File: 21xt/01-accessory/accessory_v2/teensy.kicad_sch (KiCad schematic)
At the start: 15 parts, among them T1 749013011, U1 DEV-16771

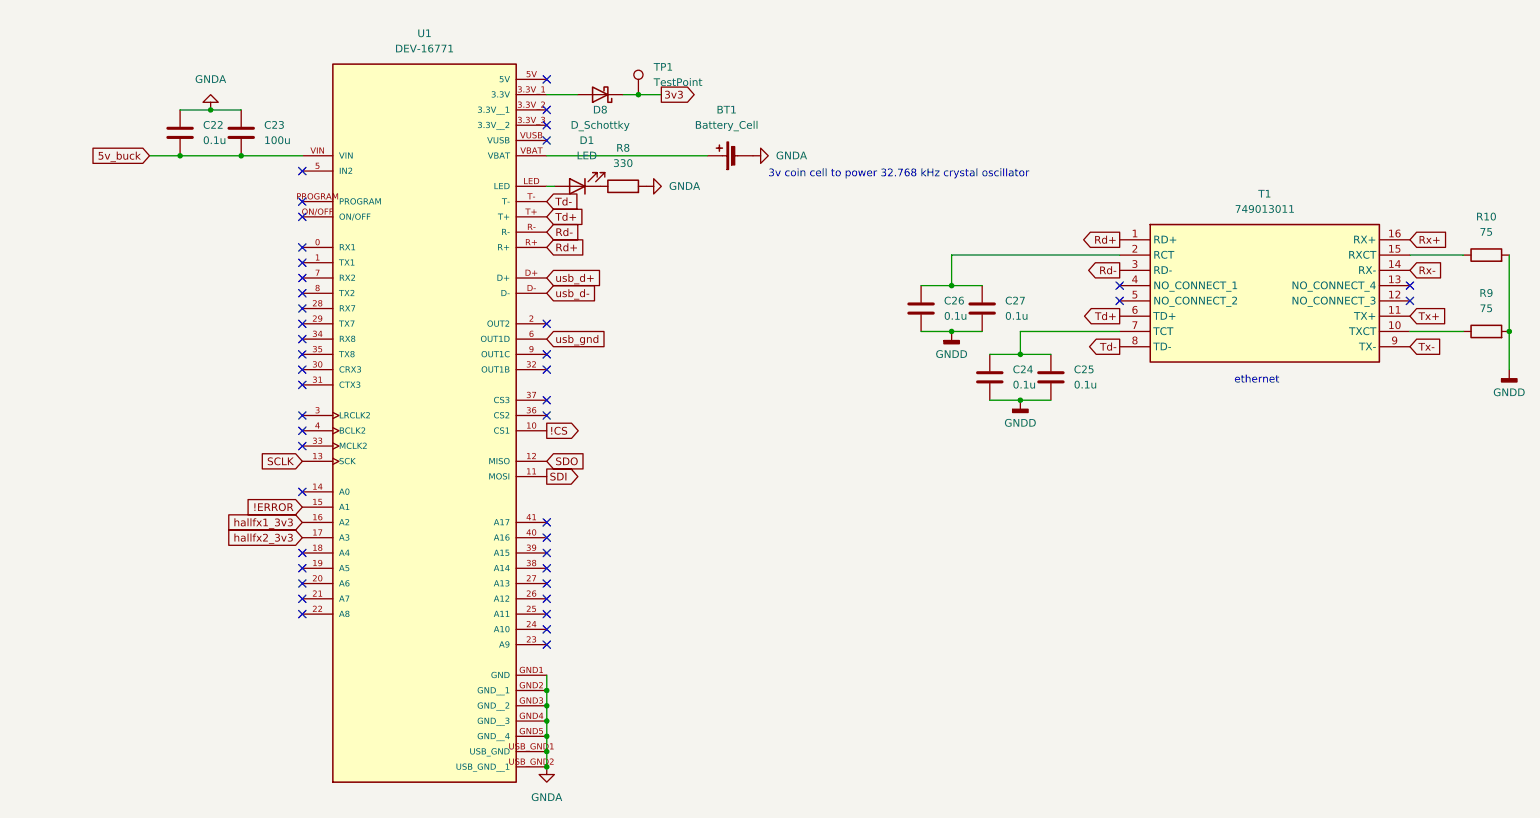
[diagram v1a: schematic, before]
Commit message: Accessory V2 schematic almost done, only missing TVS diodes and checking
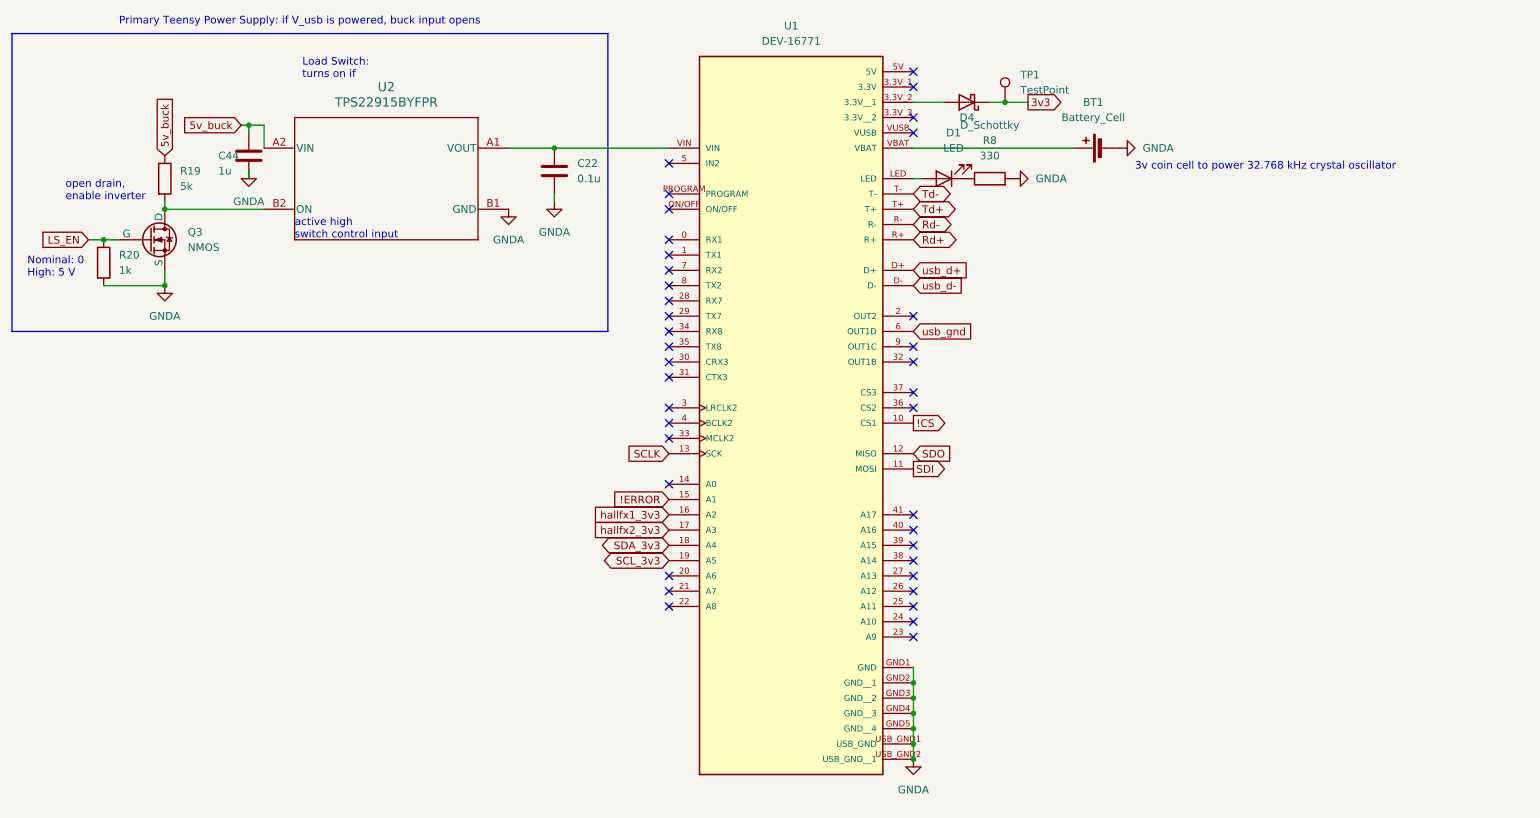
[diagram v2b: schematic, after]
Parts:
- removed C23: 100u, Capacitor_SMD:C_1206_3216Metric, symbol Device:C
- removed C24, C25, C26, C27: 0.1u, Capacitor_SMD:C_0603_1608Metric, symbol Device:C
- removed D8: D_Schottky, Diode_SMD:D_0603_1608Metric, symbol Device:D_Schottky
- removed R10, R9: 75, Resistor_SMD:R_0603_1608Metric, symbol Device:R
- removed T1: 749013011, 21xt_footprints:749013011, symbol 21xt_symbols:749013011
- added C44: 1u, Capacitor_SMD:C_0603_1608Metric, symbol Device:C
- added D4: D_Schottky, Diode_SMD:D_0603_1608Metric, symbol Device:D_Schottky
- added Q3: NMOS, symbol Simulation_SPICE:NMOS
- added R19: 5k, symbol Device:R
- added R20: 1k, symbol Device:R
- added U2: TPS22915BYFPR, 21xt_footprints:YFP0004AAAA, symbol 21xt_symbols:TPS22915BYFPR
- BT1: footprint (none) -> Battery:BatteryHolder_Keystone_1060_1x2032
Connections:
- net 3v3: now also D4.1 (K)
- net 5v_buck: now also C44.2, R19.1, U2.A2 (VIN); no longer C22.2, U1.VIN
- net GNDA: now also C44.1, Q3.3 (S), R20.2, U2.B1 (GND)
- net SDA_3v3: now reaches U1.18 (A4)
- net SCL_3v3: now reaches U1.19 (A5)
- net at U1.3.3V_2 (3.3V__1): now also D4.2 (A)
- new net: Q3.1 (D), R19.2, U2.B2 (ON)
- new net: C22.2, U1.VIN, U2.A1 (VOUT)
- new net LS_EN: Q3.2 (G), R20.1
- no-connect marks 44 -> 38
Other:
- note added: "Load Switch: turns on if"
- note added: "Nominal: 0 High: 5 V"
- note added: "Primary Teensy Power Supply: if V_usb is powered, buck input opens"
- note added: "active high switch control input"
- note added: "open drain, enable inverter"
- note removed: "ethernet"
- moved on the sheet: BT1, D1, R8, U1

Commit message: comments for revision added
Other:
- note added: "actually is this intended for the usb connector on the teensy? because if it is, then the usb cannot back power the board and blow up your buck converter if you leave the shottky i told you to remove, but even then, the buck converter can blow up the USB line or just overvolt it because the usb does not get disconnected"
- note added: "also if we have no power on the car, but have power on usb, will this turn on? it seems to me that if the connector is plugged in then ls_en is grounded so the gate opens, but there is no power"
- note added: "also you need to add the 4 pin m8 connector for getting the usb power to the teensy, though I suppose this functions for powering the teensy via the usb connector on the teensy board"
- note added: "i dont think these are the right connections for the usb grounding"
- note added: "i dont think you have connected all of the digital pins d4,5,6"
- note added: "i think i am impartial to the case where we are connecting to the teensy via the microusb on the board but if you wanted to have a proper load switch for the m8 connector that you are exposing, then i think you would need the load switch on that line: ie if the ls_en pin is activated then turn off the m8 power,"
- note added: "it becomes a bit more complicated if you wanted to support the USB connector on the board, in that case, you probably have to have the USB power always be the source for everything when its plugged in or have to snip the trace in order to control that connection, at the very least i think you have to model the m8 connector and determine which of that connector and the big bulkhead are dominant an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"
- note added: "or hallfx3"
- note added: "shouldnt the buck converter have precedent over the usb power for example: if the usb is higher voltage than buck, then the signals will exceed the threshold for levels on the usb, if the buck converter is higher though, then the signalling on the usb side may not reach high enough. also, we want no interruption when you plug in and need to switch tho id if that is significant"
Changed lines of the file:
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@@
     (stroke (width 0) (type default))
+  )
+  (arc (start 313.69 53.34) (mid 254.2256 96.5696) (end 181.61 85.09)
+    (stroke (width 0) (type default))
+    (fill (type none))
+  )
+  (arc (start 312.42 54.61) (mid 243.3139 81.7468) (end 175.26 52.07)
+    (stroke (width 0) (type default))
+    (fill (type none))
+  )
+  (arc (start -6.35 22.86) (mid 25.5167 29.747) (end 43.18 57.15)
+    (stroke (width 0) (type default))
+    (fill (type none))
+  )
+  (arc (start 313.69 109.22) (mid 222.2951 150.7967) (end 128.27 115.57)
+    (stroke (width 0) (type default))
+    (fill (type none))
+  )
+  (arc (start 313.69 54.61) (mid 263.349 134.2339) (end 171.45 154.94)
+    (stroke (width 0) (type default))
+    (fill (type none))
   )
   (rectangle (start 27.94 35.56) (end 127 85.09)
@@
     (effects (font (size 1.27 1.27)) (justify left bottom))
   )
+  (text "it becomes a bit more complicated if you wanted to support the USB\nconnector on the board, in that case, you probably have to have\nthe USB power always be the source for everything when its plugged\nin or have to snip the trace in order to control that connection,\nat the very least i think you have to model the m8 connector\nand determine which of that connector and the big bulkhead are dominant\nand possible just ignore the usb, but maximally, this would require two\nload switches and possibly snipping the connection, but i think we can\nget around that by just asuming the usb connector is only for off board\ncases and the primary modality of programming this guy is through the\nm8 connector"
+    (at -74.93 127 0)
+    (effects (font (size 1.27 1.27)) (justify left bottom))
+  )
   (text "Nominal: 0\nHigh: 5 V" (at 30.48 76.2 0)
+    (effects (font (size 1.27 1.27)) (justify left bottom))
+  )
+  (text "shouldnt the buck converter have precedent over the usb power\nfor example: if the usb is higher voltage than buck, then\nthe signals will exceed the threshold for levels on the usb,\nif the buck converter is higher though, then the signalling \non the usb side may not reach high enough. also, we want no\ninterruption when you plug in and need to switch tho id if \nthat is significant"
+    (at -71.12 21.59 0)
+    (effects (font (size 1.27 1.27)) (justify left bottom))
+  )
+  (text "actually is this intended for the usb connector\non the teensy? because if it is, then the usb\ncannot back power the board and blow up your \nbuck converter if you leave the shottky i told\nyou to remove, but even then, the buck converter\ncan blow up the USB line or just overvolt it\nbecause the usb does not get disconnected"
+    (at -80.01 72.39 0)
     (effects (font (size 1.27 1.27)) (justify left bottom))
   )
@@
     (effects (font (size 1.27 1.27)) (justify left bottom))
   )
+  (text "or hallfx3" (at 313.69 114.3 0)
+    (effects (font (size 1.27 1.27)) (justify left bottom))
+  )
+  (text "i dont think you have connected all of the digital pins d4,5,6"
+    (at 313.69 110.49 0)
+    (effects (font (size 1.27 1.27)) (justify left bottom))
+  )
+  (text "also you need to add the 4 pin m8 connector\nfor getting the usb power to the teensy,\nthough I suppose this functions for powering the teensy\nvia the usb connector on the teensy board"
+    (at -69.85 50.8 0)
+    (effects (font (size 1.27 1.27)) (justify left bottom))
+  )
+  (text "i think i am impartial to the case where we are connecting\nto the teensy via the microusb on the board but\nif you wanted to have a proper load switch for the\nm8 connector that you are exposing, then i think you would need\nthe load switch on that line: ie if the ls_en pin is activated\nthen turn off the m8 power,\n"
+    (at -78.74 97.79 0)
+    (effects (font (size 1.27 1.27)) (justify left bottom))
+  )
+  (text "i dont think these are the right connections for the usb grounding"
+    (at 317.5 54.61 0)
+    (effects (font (size 1.27 1.27)) (justify left bottom))
+  )
+  (text "also if we have no power on the car, but have power on usb, will this turn on?\nit seems to me that if the connector is plugged in then\nls_en is grounded so the gate opens, but there is no power "
+    (at -76.2 34.29 0)
+    (effects (font (size 1.27 1.27)) (justify left bottom))
+  )

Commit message: Addressed some comments
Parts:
- added R43, R44, R45, R47: 22, symbol Device:R
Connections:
- net !ERROR: now also U1.14 (A0); no longer U1.15 (A1)
- net SDI: now also R44.2; no longer U1.11 (MOSI)
- net D4_3v3: now reaches U1.0 (RX1)
- net D3_3v3: now reaches U1.1 (TX1)
- net D2_3v3: now reaches U1.26 (A12)
- net D1_3v3: now reaches U1.27 (A13)
- net !RESET: now reaches U1.35 (TX8)
- net !LDAC: now reaches U1.36 (CS2)
- net at U1.37 (CS3): now also R47.1
- net D6_3v3: now reaches U1.7 (RX2)
- net D5_3v3: now reaches U1.8 (TX2)
- net !CS: no longer names the net of U1.10 (CS1)
- net !CS: now also R45.1
- net SCLK: no longer names the net of U1.13 (SCK)
- net SCLK: now also R43.2
- net SDO renamed SDO_ADC
- net hallfx1_3v3: no longer names the net of U1.16 (A2)
- net hallfx2_3v3: no longer names the net of U1.17 (A3)
- new net: R44.1, U1.11 (MOSI)
- new net !CS_ADC: R45.2
- new net !CS_DAC: R47.2
- new net SCK: R43.1
- no-connect marks 38 -> 28
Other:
- note removed: "i dont think you have connected all of the digital pins d4,5,6"
- note removed: "or hallfx3"

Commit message: added files
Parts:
- removed D4: D_Schottky, Diode_SMD:D_0603_1608Metric, symbol Device:D_Schottky
- removed Q3: NMOS, symbol Simulation_SPICE:NMOS
- added Q3: BSS138, Package_TO_SOT_SMD:SOT-23, symbol Transistor_FET:BSS138
- C22, C44: footprint Capacitor_SMD:C_0603_1608Metric -> Capacitor_SMD:C_0402_1005Metric
- R19, R20, R43, R44, R45, R47: footprint (none) -> Resistor_SMD:R_0603_1608Metric
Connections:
- net 3v3: now also U1.3.3V_2 (3.3V__1)
- net GNDA: now also Q3.2 (S)
- net LS_EN: now also Q3.1 (G)
- net at R19.2, U2.B2 (ON): now also Q3.3 (D)
- net at U1.23 (A9): now also D1.2 (A)
- net GPIO/INT1_3v3: now reaches U1.24 (A10)
- net GPIO/INT2_3v3: now reaches U1.25 (A11)
- net at U1.LED: no longer D1.2 (A)
- net 5v_usb: now reaches U1.VUSB
- net usb_d+: no longer names the net of U1.D+
- net usb_d-: no longer names the net of U1.D-
- net usb_gnd: no longer names the net of U1.6 (OUT1D)
- no-connect marks 28 -> 31
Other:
- note added: "LS_EN = 0 -> Buck converter is connected LS_EN = 5 -> Buck converter is not connected"
- note removed: "Nominal: 0 High: 5 V"
- note removed: "actually is this intended for the usb connector on the teensy? because if it is, then the usb cannot back power the board and blow up your buck converter if you leave the shottky i told you to remove, but even then, the buck converter can blow up the USB line or just overvolt it because the usb does not get disconnected"
- note removed: "also if we have no power on the car, but have power on usb, will this turn on? it seems to me that if the connector is plugged in then ls_en is grounded so the gate opens, but there is no power"
- note removed: "also you need to add the 4 pin m8 connector for getting the usb power to the teensy, though I suppose this functions for powering the teensy via the usb connector on the teensy board"
- note removed: "i dont think these are the right connections for the usb grounding"
- note removed: "i think i am impartial to the case where we are connecting to the teensy via the microusb on the board but if you wanted to have a proper load switch for the m8 connector that you are exposing, then i think you would need the load switch on that line: ie if the ls_en pin is activated then turn off the m8 power,"
- note removed: "it becomes a bit more complicated if you wanted to support the USB connector on the board, in that case, you probably have to have the USB power always be the source for everything when its plugged in or have to snip the trace in order to control that connection, at the very least i think you have to model the m8 connector and determine which of that connector and the big bulkhead are dominant an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"
- note removed: "shouldnt the buck converter have precedent over the usb power for example: if the usb is higher voltage than buck, then the signals will exceed the threshold for levels on the usb, if the buck converter is higher though, then the signalling on the usb side may not reach high enough. also, we want no interruption when you plug in and need to switch tho id if that is significant"

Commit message: some work, a bit scuffed
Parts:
- removed Q3: BSS138, Package_TO_SOT_SMD:SOT-23, symbol Transistor_FET:BSS138
- added Q3: NMOS, Package_TO_SOT_SMD:SOT-23-3, symbol Simulation_SPICE:NMOS
- added R41, R42, R46, R48, R49: 20R, Resistor_SMD:R_0402_1005Metric, symbol Device:R
- BT1: footprint Battery:BatteryHolder_Keystone_1060_1x2032 -> 21xt_footprints:1220 holder
- R19, R20, R8: footprint Resistor_SMD:R_0603_1608Metric -> Resistor_SMD:R_0402_1005Metric
- R43, R44, R45, R47: value 22 -> 20R; footprint Resistor_SMD:R_0603_1608Metric -> Resistor_SMD:R_0402_1005Metric
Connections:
- net !ERROR: now also U1.30 (CRX3); no longer U1.14 (A0)
- net !LDAC: now also R48.1; no longer U1.36 (CS2)
- net 3v3: now also U1.3.3V_3 (3.3V__2)
- net D1_3v3: now also R46.1
- net D2_3v3: now also R47.1
- net D3_3v3: now also R44.1, U1.39 (A15); no longer U1.1 (TX1)
- net D4_3v3: now also R45.1, U1.38 (A14); no longer U1.0 (RX1)
- net D5_3v3: now also U1.41 (A17); no longer U1.8 (TX2)
- net D6_3v3: now also U1.40 (A16); no longer U1.7 (RX2)
- net GNDA: no longer BT1.2 (-), C22.1, C44.1, R20.2, U1.GND1 (GND), U1.GND2 (GND__1), U1.GND3 (GND__2), U1.GND4 (GND__3), U1.GND5 (GND__4), U1.USB_GND1 (USB_GND), U1.USB_GND2 (USB_GND__1), U2.B1 (GND)
- net GPIO/INT1_3v3: now also U1.0 (RX1); no longer U1.24 (A10)
- net GPIO/INT2_3v3: now also U1.1 (TX1); no longer U1.25 (A11)
- net LS_EN: now also Q3.2 (G)
- net at U1.37 (CS3): no longer R47.1
- net at U1.23 (A9): no longer D1.2 (A)
- net at U1.10 (CS1): now also R49.1; no longer R45.1
- net at R19.2, U2.B2 (ON): now also Q3.1 (D)
- net at U1.11 (MOSI): now also R42.1; no longer R44.1
- net SYNC: now reaches U1.31 (CTX3)
- net at U1.32 (OUT1B): now also R48.2
- net usb_d+: now reaches U1.D+
- net usb_d-: now reaches U1.D-
- net at U1.LED: now also D1.2 (A)
- net !CS_ADC renamed CS-DAC
- net !CS_DAC renamed MOSI1
- net !RESET: no longer names the net of U1.35 (TX8)
- net 5v_usb: no longer names the net of U1.VUSB
- net SCK renamed SCLK
- net SDI renamed MISO1
- net SDO_ADC: no longer names the net of U1.12 (MISO)
- net SDO_ADC: now also R41.1
- new net !CS: R49.2
- new net GNDD: BT1.2 (-), C22.1, C44.1, Q3.3 (S), R20.2, U1.GND1 (GND), U1.GND2 (GND__1), U1.GND3 (GND__2), U1.GND4 (GND__3), U1.GND5 (GND__4), U2.B1 (GND)
- new net MISO: R41.2
- new net MOSI: R42.2
- new net SCLK1: R46.2
- new net usb_gnd: U1.USB_GND1 (USB_GND), U1.USB_GND2 (USB_GND__1)
- no-connect marks 31 -> 30
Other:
- note added: "Nominal: 0 High: 5 V"
- note added: "actually is this intended for the usb connector on the teensy? because if it is, then the usb cannot back power the board and blow up your buck converter if you leave the shottky i told you to remove, but even then, the buck converter can blow up the USB line or just overvolt it because the usb does not get disconnected"
- note added: "also if we have no power on the car, but have power on usb, will this turn on? it seems to me that if the connector is plugged in then ls_en is grounded so the gate opens, but there is no power"
- note added: "also you need to add the 4 pin m8 connector for getting the usb power to the teensy, though I suppose this functions for powering the teensy via the usb connector on the teensy board"
- note added: "i dont think these are the right connections for the usb grounding"
- note added: "i think i am impartial to the case where we are connecting to the teensy via the microusb on the board but if you wanted to have a proper load switch for the m8 connector that you are exposing, then i think you would need the load switch on that line: ie if the ls_en pin is activated then turn off the m8 power,"
- note added: "it becomes a bit more complicated if you wanted to support the USB connector on the board, in that case, you probably have to have the USB power always be the source for everything when its plugged in or have to snip the trace in order to control that connection, at the very least i think you have to model the m8 connector and determine which of that connector and the big bulkhead are dominant an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"
- note added: "shouldnt the buck converter have precedent over the usb power for example: if the usb is higher voltage than buck, then the signals will exceed the threshold for levels on the usb, if the buck converter is higher though, then the signalling on the usb side may not reach high enough. also, we want no interruption when you plug in and need to switch tho id if that is significant"
- note removed: "LS_EN = 0 -> Buck converter is connected LS_EN = 5 -> Buck converter is not connected"
- moved on the sheet: C22, C44, R19, R20, U2
